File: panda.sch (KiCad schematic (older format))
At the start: 26 parts, among them J1 USB, J2 ICSP, U1 ATMEGA328-P, U2 MAX7219, Y1 12MHz

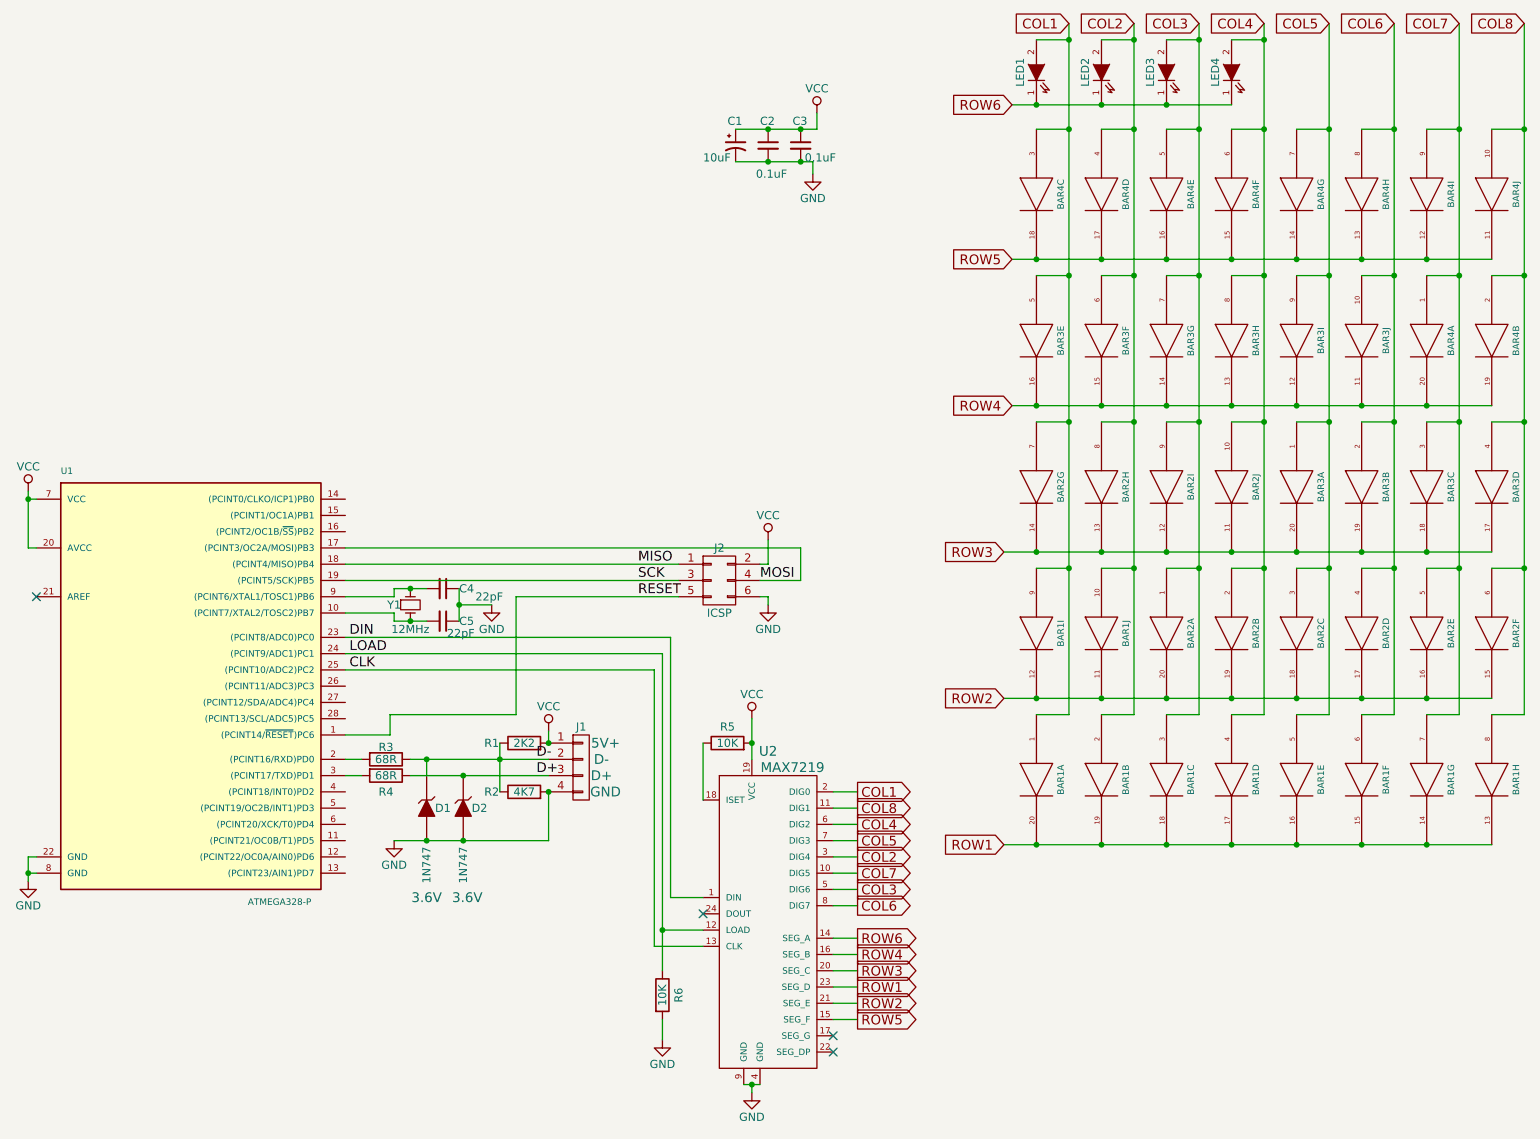
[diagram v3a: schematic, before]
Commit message: Slight mods to accomodate firmware.
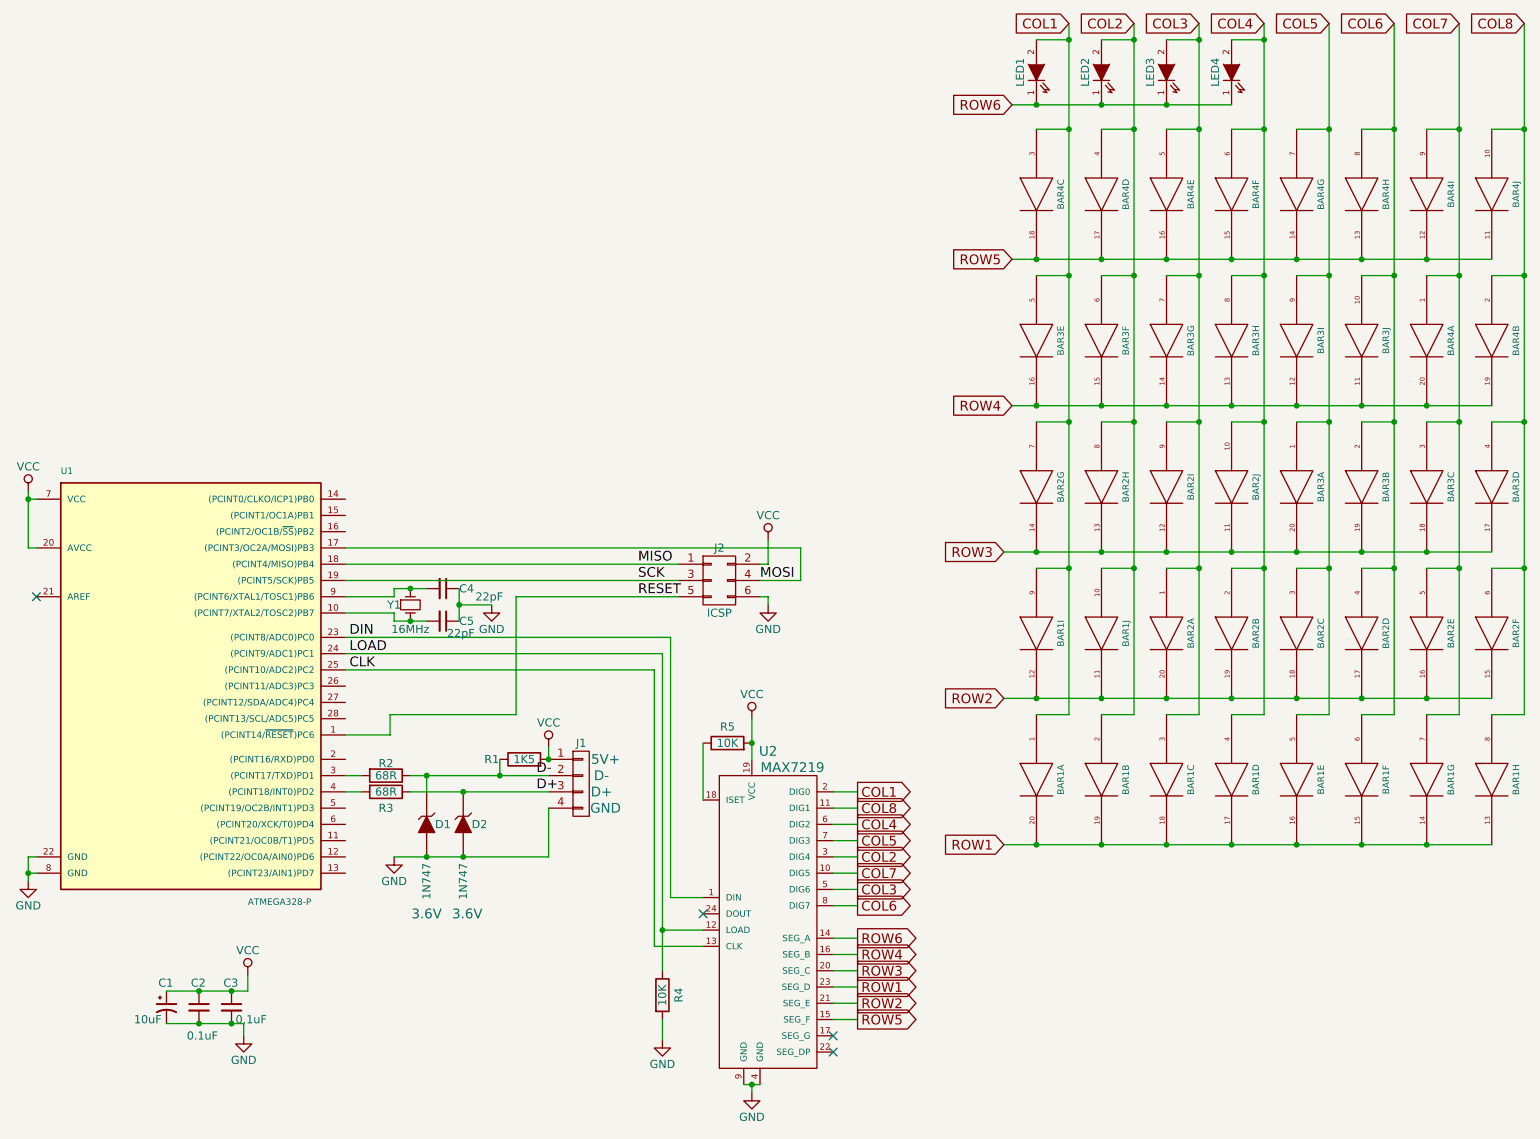
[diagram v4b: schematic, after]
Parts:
- removed R2: 4K7, custom_resistors:Resistor_Horizontal_RM7.62mm, symbol R
- R1: value 2K2 -> 1K5; footprint custom_resistors:Resistor_Horizontal_RM7.62mm -> My_Resistors_ThroughHole:Resistor_Horizontal_RM7.62mm
- R2: renamed from R3; footprint custom_resistors:Resistor_Horizontal_RM7.62mm -> My_Resistors_ThroughHole:Resistor_Horizontal_RM7.62mm
- R3: renamed from R4; footprint custom_resistors:Resistor_Horizontal_RM7.62mm -> My_Resistors_ThroughHole:Resistor_Horizontal_RM7.62mm
- R4: renamed from R6; footprint custom_resistors:Resistor_Horizontal_RM7.62mm -> My_Resistors_ThroughHole:Resistor_Horizontal_RM7.62mm
- R5: footprint custom_resistors:Resistor_Horizontal_RM7.62mm -> My_Resistors_ThroughHole:Resistor_Horizontal_RM7.62mm
- Y1: value 12MHz -> 16MHz
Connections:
- net at U1.2 ((PCINT16/RXD)PD0): no longer R2.2
- net at U1.3 ((PCINT17/TXD)PD1): now also R2.2; no longer R3.2
- net at U1.4 ((PCINT18/INT0)PD2): now also R3.2
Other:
- moved on the sheet: C1, C2, C3, D1, D2, J1, R1, R2, R3
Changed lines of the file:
@@
 L ZENER D1
 U 1 1 564A8ADA
-P 3250 6000
-F 0 "D1" V 3250 6100 50  0000 C CNN
-F 1 "1N747" H 3600 6000 50  0000 C CNN
-F 2 "Diodes_ThroughHole:Diode_DO-35_SOD27_Horizontal_RM10" H 3250 6000 60  0001 C CNN
-F 3 "" H 3250 6000 60  0000 C CNN
-F 4 "3.6V" V 3800 6000 60  0000 C CNN "Voltage"
-	1    3250 6000
+P 3250 6100
+F 0 "D1" V 3250 6200 50  0000 C CNN
+F 1 "1N747" H 3600 6100 50  0000 C CNN
+F 2 "Diodes_ThroughHole:Diode_DO-35_SOD27_Horizontal_RM10" H 3250 6100 60  0001 C CNN
+F 3 "" H 3250 6100 60  0000 C CNN
+F 4 "3.6V" V 3800 6100 60  0000 C CNN "Voltage"
+	1    3250 6100
 	0    1    1    0
 $EndComp
@@
 L CONN_01X04 J1
 U 1 1 564A9ED0
-P 4200 5750
-F 0 "J1" H 4200 6000 50  0000 C CNN
-F 1 "USB" V 4300 5750 50  0001 C CNN
-F 2 "Pin_Headers:Pin_Header_Straight_1x04" H 4200 5750 60  0001 C CNN
-F 3 "" H 4200 5750 60  0000 C CNN
-F 4 "5V+" H 4350 5900 60  0000 C CNN "Pin1"
-F 5 "D-" H 4325 5800 60  0000 C CNN "Pin2"
-F 6 "D+" H 4325 5700 60  0000 C CNN "Pin3"
-F 7 "GND" H 4350 5600 60  0000 C CNN "Pin4"
-	1    4200 5750
+P 4200 5850
+F 0 "J1" H 4200 6100 50  0000 C CNN
+F 1 "USB" V 4300 5850 50  0001 C CNN
+F 2 "Pin_Headers:Pin_Header_Straight_1x04" H 4200 5850 60  0001 C CNN
+F 3 "" H 4200 5850 60  0000 C CNN
+F 4 "5V+" H 4350 6000 60  0000 C CNN "Pin1"
+F 5 "D-" H 4325 5900 60  0000 C CNN "Pin2"
+F 6 "D+" H 4325 5800 60  0000 C CNN "Pin3"
+F 7 "GND" H 4350 5700 60  0000 C CNN "Pin4"
+	1    4200 5850
 	1    0    0    -1
 $EndComp
@@
 L ZENER D2
 U 1 1 564ABD9A
-P 3475 6000
-F 0 "D2" V 3475 6100 50  0000 C CNN
-F 1 "1N747" H 3825 6000 50  0000 C CNN
-F 2 "Diodes_ThroughHole:Diode_DO-35_SOD27_Horizontal_RM10" H 3475 6000 60  0001 C CNN
-F 3 "" H 3475 6000 60  0000 C CNN
-F 4 "3.6V" V 4025 6025 60  0000 C CNN "Voltage"
-	1    3475 6000
-	0    1    1    0
-$EndComp
-Wire Wire Line
-	3050 6200 4000 6200
-Wire Wire Line
-	4000 6200 4000 5900
-Connection ~ 3475 6200
+P 3475 6100
+F 0 "D2" V 3475 6200 50  0000 C CNN
+F 1 "1N747" H 3825 6100 50  0000 C CNN
+F 2 "Diodes_ThroughHole:Diode_DO-35_SOD27_Horizontal_RM10" H 3475 6100 60  0001 C CNN
+F 3 "" H 3475 6100 60  0000 C CNN
+F 4 "3.6V" V 4025 6125 60  0000 C CNN "Voltage"
+	1    3475 6100
+	0    1    1    0
+$EndComp
+Wire Wire Line
+	3050 6300 4000 6300
+Wire Wire Line
+	4000 6300 4000 6000
+Connection ~ 3475 6300
+Wire Wire Line
+	3150 5900 4000 5900
 Wire Wire Line
 	3150 5800 4000 5800
-Wire Wire Line
-	3150 5700 4000 5700
-$Comp
-L R R4
+$Comp
+L R R3
 U 1 1 564AC1D1
+P 3000 5900
+F 0 "R3" V 3100 5900 50  0000 C CNN
+F 1 "68R" V 3000 5900 50  0000 C CNN
+F 2 "My_Resistors_ThroughHole:Resistor_Horizontal_RM7.62mm" V 2930 5900 30  0001 C CNN
+F 3 "" H 3000 5900 30  0000 C CNN
+	1    3000 5900
+	0    1    1    0
+$EndComp
+Wire Wire Line
+	3250 5800 3250 5900
+$Comp
+L R R2
+U 1 1 564AD8DE
 P 3000 5800
-F 0 "R4" V 3100 5800 50  0000 C CNN
+F 0 "R2" V 2925 5800 50  0000 C CNN
 F 1 "68R" V 3000 5800 50  0000 C CNN
-F 2 "custom_resistors:Resistor_Horizontal_RM7.62mm" V 2930 5800 30  0001 C CNN
+F 2 "My_Resistors_ThroughHole:Resistor_Horizontal_RM7.62mm" V 2930 5800 30  0001 C CNN
 F 3 "" H 3000 5800 30  0000 C CNN
 	1    3000 5800
 	0    1    1    0
 $EndComp
-Wire Wire Line
-	3250 5700 3250 5800
-$Comp
-L R R2
-U 1 1 564AC920
-P 3850 5900
-F 0 "R2" V 3850 6100 50  0000 C CNN
-F 1 "4K7" V 3850 5900 50  0000 C CNN
-F 2 "custom_resistors:Resistor_Horizontal_RM7.62mm" V 3780 5900 30  0001 C CNN
-F 3 "" H 3850 5900 30  0000 C CNN
-	1    3850 5900
-	0    -1   -1   0
-$EndComp
-$Comp
-L R R3
-U 1 1 564AD8DE
-P 3000 5700
-F 0 "R3" V 2925 5700 50  0000 C CNN
-F 1 "68R" V 3000 5700 50  0000 C CNN
-F 2 "custom_resistors:Resistor_Horizontal_RM7.62mm" V 2930 5700 30  0001 C CNN
-F 3 "" H 3000 5700 30  0000 C CNN
-	1    3000 5700
-	0    1    1    0
-$EndComp
-Connection ~ 3250 6200
+Connection ~ 3250 6300
 $Comp
 L GND #PWR01
 U 1 1 564B070E
-P 3050 6200
-F 0 "#PWR01" H 3050 5950 50  0001 C CNN
-F 1 "GND" H 3050 6050 50  0000 C CNN
-F 2 "" H 3050 6200 60  0000 C CNN
-F 3 "" H 3050 6200 60  0000 C CNN
-	1    3050 6200
+P 3050 6300
+F 0 "#PWR01" H 3050 6050 50  0001 C CNN
+F 1 "GND" H 3050 6150 50  0000 C CNN
+F 2 "" H 3050 6300 60  0000 C CNN
+F 3 "" H 3050 6300 60  0000 C CNN
+	1    3050 6300
 	1    0    0    -1
 $EndComp
@@
 L VCC #PWR02
 U 1 1 564B60A8
-P 4000 5525
-F 0 "#PWR02" H 4000 5375 50  0001 C CNN
-F 1 "VCC" H 4000 5675 50  0000 C CNN
-F 2 "" H 4000 5525 60  0000 C CNN
-F 3 "" H 4000 5525 60  0000 C CNN
-	1    4000 5525
+P 4000 5625
+F 0 "#PWR02" H 4000 5475 50  0001 C CNN
+F 1 "VCC" H 4000 5775 50  0000 C CNN
+F 2 "" H 4000 5625 60  0000 C CNN
+F 3 "" H 4000 5625 60  0000 C CNN
+	1    4000 5625
 	1    0    0    -1
 $EndComp
@@
 F 0 "R5" V 5200 5600 50  0000 C CNN
 F 1 "10K" V 5100 5600 50  0000 C CNN
-F 2 "custom_resistors:Resistor_Horizontal_RM7.62mm" V 5030 5600 30  0001 C CNN
+F 2 "My_Resistors_ThroughHole:Resistor_Horizontal_RM7.62mm" V 5030 5600 30  0001 C CNN
 F 3 "" H 5100 5600 30  0000 C CNN
 	1    5100 5600
@@
 	4650 5150 4650 6850
 $Comp
-L R R6
+L R R4
 U 1 1 564D834E
 P 4700 7150
-F 0 "R6" V 4800 7150 50  0000 C CNN
+F 0 "R4" V 4800 7150 50  0000 C CNN
 F 1 "10K" V 4700 7150 50  0000 C CNN
-F 2 "custom_resistors:Resistor_Horizontal_RM7.62mm" V 4630 7150 30  0001 C CNN
+F 2 "My_Resistors_ThroughHole:Resistor_Horizontal_RM7.62mm" V 4630 7150 30  0001 C CNN
 F 3 "" H 4700 7150 30  0000 C CNN
 	1    4700 7150
@@
 P 3150 4750
 F 0 "Y1" V 3150 4650 50  0000 C CNN
-F 1 "12MHz" V 3300 4750 50  0000 C CNN
+F 1 "16MHz" V 3300 4750 50  0000 C CNN
 F 2 "Crystals:Crystal_HC49-U_Vertical" H 3150 4750 60  0001 C CNN
 F 3 "" H 3150 4750 60  0000 C CNN
@@
 	4650 5150 2750 5150
 Wire Wire Line
-	2850 5700 2750 5700
-Wire Wire Line
-	2750 5800 2850 5800
-Connection ~ 3250 5700
-Connection ~ 3475 5800
+	2850 5800 2750 5800
+Wire Wire Line
+	2750 5900 2850 5900
+Connection ~ 3250 5800
+Connection ~ 3475 5900
 $Comp
 L R R1
 U 1 1 5650796C
-P 3850 5600
-F 0 "R1" V 3850 5800 50  0000 C CNN
-F 1 "2K2" V 3850 5600 50  0000 C CNN
-F 2 "custom_resistors:Resistor_Horizontal_RM7.62mm" V 3780 5600 30  0001 C CNN
-F 3 "" H 3850 5600 30  0000 C CNN
-	1    3850 5600
+P 3850 5700
+F 0 "R1" V 3850 5900 50  0000 C CNN
+F 1 "1K5" V 3850 5700 50  0000 C CNN
+F 2 "My_Resistors_ThroughHole:Resistor_Horizontal_RM7.62mm" V 3780 5700 30  0001 C CNN
+F 3 "" H 3850 5700 30  0000 C CNN
+	1    3850 5700
 	0    -1   -1   0
 $EndComp
-Wire Wire Line
-	3700 5600 3700 5900
-Connection ~ 3700 5700
+Connection ~ 3700 5800
 Wire Wire Line
 	3025 5550 2750 5550
@@
 L VCC #PWR011
 U 1 1 5651069A
-P 5650 1725
-F 0 "#PWR011" H 5650 1575 50  0001 C CNN
-F 1 "VCC" H 5650 1875 50  0000 C CNN
-F 2 "" H 5650 1725 60  0000 C CNN
-F 3 "" H 5650 1725 60  0000 C CNN
-	1    5650 1725
+P 2150 7025
+F 0 "#PWR011" H 2150 6875 50  0001 C CNN
+F 1 "VCC" H 2150 7175 50  0000 C CNN
+F 2 "" H 2150 7025 60  0000 C CNN
+F 3 "" H 2150 7025 60  0000 C CNN
+	1    2150 7025
 	1    0    0    -1
 $EndComp
@@
 L GND #PWR012
 U 1 1 56510724
-P 5625 2100
-F 0 "#PWR012" H 5625 1850 50  0001 C CNN
-F 1 "GND" H 5625 1950 50  0000 C CNN
-F 2 "" H 5625 2100 60  0000 C CNN
-F 3 "" H 5625 2100 60  0000 C CNN
-	1    5625 2100
+P 2125 7400
+F 0 "#PWR012" H 2125 7150 50  0001 C CNN
+F 1 "GND" H 2125 7250 50  0000 C CNN
+F 2 "" H 2125 7400 60  0000 C CNN
+F 3 "" H 2125 7400 60  0000 C CNN
+	1    2125 7400
 	1    0    0    -1
 $EndComp
@@
 L C_Small C2
 U 1 1 56510AC6
-P 5350 1925
-F 0 "C2" H 5300 2075 50  0000 L CNN
-F 1 "0.1uF" H 5275 1750 50  0000 L CNN
-F 2 "Capacitors_ThroughHole:C_Rect_L4_W2.5_P2.5" H 5350 1925 60  0001 C CNN
-F 3 "" H 5350 1925 60  0000 C CNN
-	1    5350 1925
+P 1850 7225
+F 0 "C2" H 1800 7375 50  0000 L CNN
+F 1 "0.1uF" H 1775 7050 50  0000 L CNN
+F 2 "Capacitors_ThroughHole:C_Rect_L4_W2.5_P2.5" H 1850 7225 60  0001 C CNN
+F 3 "" H 1850 7225 60  0000 C CNN
+	1    1850 7225
 	1    0    0    -1
 $EndComp
@@
 L CP1_Small C1
 U 1 1 56510C65
-P 5150 1925
-F 0 "C1" H 5100 2075 50  0000 L CNN
-F 1 "10uF" H 4950 1850 50  0000 L CNN
-F 2 "Capacitors_ThroughHole:C_Radial_D5_L6_P2.5" H 5150 1925 60  0001 C CNN
-F 3 "" H 5150 1925 60  0000 C CNN
-	1    5150 1925
+P 1650 7225
+F 0 "C1" H 1600 7375 50  0000 L CNN
+F 1 "10uF" H 1450 7150 50  0000 L CNN
+F 2 "Capacitors_ThroughHole:C_Radial_D5_L6_P2.5" H 1650 7225 60  0001 C CNN
+F 3 "" H 1650 7225 60  0000 C CNN
+	1    1650 7225
 	1    0    0    -1
 $EndComp
@@
 L C_Small C3
 U 1 1 565126CE
-P 5550 1925
-F 0 "C3" H 5500 2075 50  0000 L CNN
-F 1 "0.1uF" H 5575 1850 50  0000 L CNN
-F 2 "Capacitors_ThroughHole:C_Rect_L4_W2.5_P2.5" H 5550 1925 60  0001 C CNN
-F 3 "" H 5550 1925 60  0000 C CNN
-	1    5550 1925
-	1    0    0    -1
-$EndComp
-Wire Wire Line
-	5150 2025 5625 2025
-Connection ~ 5350 2025
-Wire Wire Line
-	5150 1825 5650 1825
-Connection ~ 5350 1825
-Wire Wire Line
-	5650 1825 5650 1725
-Connection ~ 5550 1825
-Wire Wire Line
-	5625 2025 5625 2100
-Connection ~ 5550 2025
-Connection ~ 4000 5900
-Wire Wire Line
-	4000 5525 4000 5600
-Connection ~ 4000 5600
+P 2050 7225
+F 0 "C3" H 2000 7375 50  0000 L CNN
+F 1 "0.1uF" H 2075 7150 50  0000 L CNN
+F 2 "Capacitors_ThroughHole:C_Rect_L4_W2.5_P2.5" H 2050 7225 60  0001 C CNN
+F 3 "" H 2050 7225 60  0000 C CNN
+	1    2050 7225
+	1    0    0    -1
+$EndComp
+Wire Wire Line
+	1650 7325 2125 7325
+Connection ~ 1850 7325
+Wire Wire Line
+	1650 7125 2150 7125
+Connection ~ 1850 7125
+Wire Wire Line
+	2150 7125 2150 7025
+Connection ~ 2050 7125
+Wire Wire Line
+	2125 7325 2125 7400
+Connection ~ 2050 7325
+Wire Wire Line
+	4000 5625 4000 5700
+Connection ~ 4000 5700
 Text Label 2775 4950 0    60   ~ 0
 DIN
@@
 Text Label 2775 5150 0    60   ~ 0
 CLK
-Text Label 3925 5700 0    60   ~ 0
+Text Label 3925 5800 0    60   ~ 0
 D-
-Text Label 3925 5800 0    60   ~ 0
+Text Label 3925 5900 0    60   ~ 0
 D+
 Wire Wire Line
@@
 	3025 5425 3025 5550
 NoConn ~ 4950 6650
+Wire Wire Line
+	3700 5800 3700 5700
 $EndSCHEMATC

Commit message: Update tweaks.
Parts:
- U1: value ATMEGA328-P -> ATMEGA8
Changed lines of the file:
@@
 P 1750 5200
 F 0 "U1" H 1000 6450 40  0000 L BNN
-F 1 "ATMEGA328-P" H 2150 3800 40  0000 L BNN
+F 1 "ATMEGA8" H 2150 3800 40  0000 L BNN
 F 2 "Housings_DIP:DIP-28_W7.62mm" H 1750 5200 30  0001 C CIN
 F 3 "" H 1750 5200 60  0000 C CNN

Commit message: Final tweaks.
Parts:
- LED1, LED2, LED3, LED4: footprint MyLEDs:LED-5MM -> LEDs:LED-5MM
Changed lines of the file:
@@
 F 0 "LED1" H 7000 1575 50  0000 C CNN
 F 1 "LED" H 7000 1375 50  0001 C CNN
-F 2 "MyLEDs:LED-5MM" H 7000 1475 60  0001 C CNN
+F 2 "LEDs:LED-5MM" H 7000 1475 60  0001 C CNN
 F 3 "" H 7000 1475 60  0000 C CNN
 	1    7000 1475
@@
 F 0 "LED2" H 7400 1575 50  0000 C CNN
 F 1 "LED" H 7400 1375 50  0001 C CNN
-F 2 "MyLEDs:LED-5MM" H 7400 1475 60  0001 C CNN
+F 2 "LEDs:LED-5MM" H 7400 1475 60  0001 C CNN
 F 3 "" H 7400 1475 60  0000 C CNN
 	1    7400 1475
@@
 F 0 "LED3" H 7800 1575 50  0000 C CNN
 F 1 "LED" H 7800 1375 50  0001 C CNN
-F 2 "MyLEDs:LED-5MM" H 7800 1475 60  0001 C CNN
+F 2 "LEDs:LED-5MM" H 7800 1475 60  0001 C CNN
 F 3 "" H 7800 1475 60  0000 C CNN
 	1    7800 1475
@@
 F 0 "LED4" H 8200 1575 50  0000 C CNN
 F 1 "LED" H 8200 1375 50  0001 C CNN
-F 2 "MyLEDs:LED-5MM" H 8200 1475 60  0001 C CNN
+F 2 "LEDs:LED-5MM" H 8200 1475 60  0001 C CNN
 F 3 "" H 8200 1475 60  0000 C CNN
 	1    8200 1475

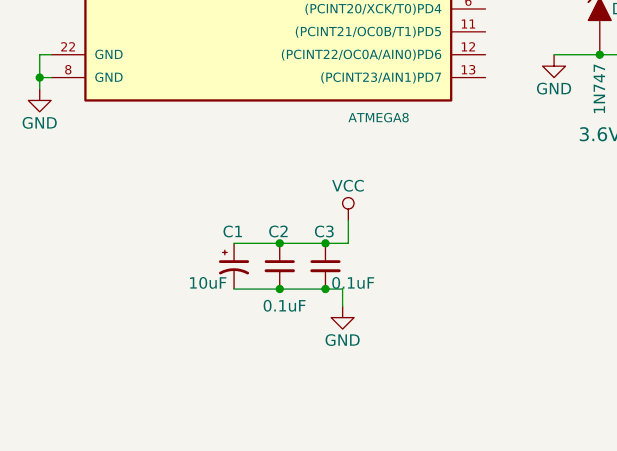
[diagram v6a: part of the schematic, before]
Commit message: Tweak value of polarized cap.
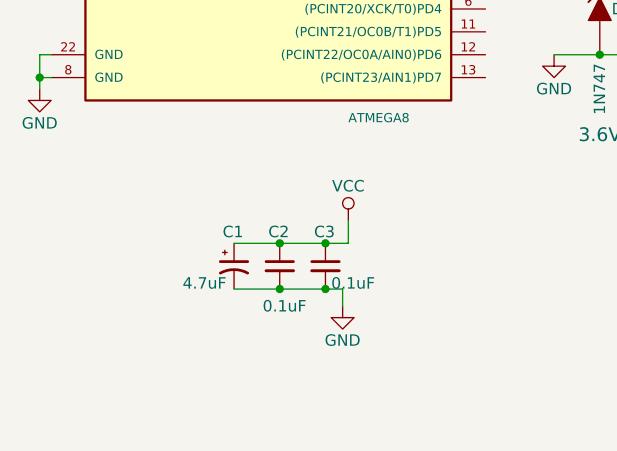
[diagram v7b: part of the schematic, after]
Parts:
- C1: value 10uF -> 4.7uF
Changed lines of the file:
@@
 P 1650 7225
 F 0 "C1" H 1600 7375 50  0000 L CNN
-F 1 "10uF" H 1450 7150 50  0000 L CNN
+F 1 "4.7uF" H 1425 7150 50  0000 L CNN
 F 2 "Capacitors_ThroughHole:C_Radial_D5_L6_P2.5" H 1650 7225 60  0001 C CNN
 F 3 "" H 1650 7225 60  0000 C CNN

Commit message: Clean up lots of messiness.
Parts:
- removed Y1: 16MHz, Crystals:Crystal_HC49-U_Vertical, symbol Crystal_Small
- added Y1: 16MHz, Crystals:Crystal_HC49-U_Vertical, symbol Crystal
- C1: footprint Capacitors_ThroughHole:C_Radial_D5_L6_P2.5 -> Capacitors_THT:CP_Radial_D5.0mm_P2.50mm
- C2, C3, C4, C5: footprint Capacitors_ThroughHole:C_Rect_L4_W2.5_P2.5 -> Capacitors_THT:C_Disc_D3.0mm_W1.6mm_P2.50mm
- D1, D2: footprint Diodes_ThroughHole:Diode_DO-35_SOD27_Horizontal_RM10 -> Diodes_THT:D_DO-35_SOD27_P7.62mm_Horizontal
- J1: footprint Pin_Headers:Pin_Header_Straight_1x04 -> Pin_Headers:Pin_Header_Straight_1x04_Pitch2.54mm
- J2: footprint Pin_Headers:Pin_Header_Straight_2x03 -> Pin_Headers:Pin_Header_Straight_2x03_Pitch2.54mm
- LED1, LED2, LED3, LED4: footprint LEDs:LED-5MM -> LEDs:LED_D5.0mm; symbol LED -> LED-RESCUE-panda
- R1, R2, R3, R4, R5: footprint My_Resistors_ThroughHole:Resistor_Horizontal_RM7.62mm -> Resistors_THT:R_Axial_DIN0204_L3.6mm_D1.6mm_P7.62mm_Horizontal
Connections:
- net GND: now also C2.1, C3.1; no longer C2.2, C3.2
- net VCC: now also C2.2, C3.2; no longer C2.1, C3.1
- net at C5.2, U1.10 ((PCINT7/XTAL2/TOSC2)PB7): now also Y1.2
- net at C4.2, U1.9 ((PCINT6/XTAL1/TOSC1)PB6): now also Y1.1
- no-connect marks 4 -> 16
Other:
- moved on the sheet: J2, R1
